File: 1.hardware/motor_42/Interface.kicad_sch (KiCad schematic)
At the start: 0 parts

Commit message: 중간 저장
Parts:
- added C15: 0.1uF/50V, symbol Device:C_Small_US
- added C16: 10uF/16V, symbol Device:C_Small_US
- added U2: MT6816CT, Package_SO:SO-8_3.9x4.9mm_P1.27mm, symbol Sensor_Magnetic:MT6816CT
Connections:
- new net 3V3: C15.1, C16.1, U2.2 (HVPP), U2.4 (VDD)
- new net GND: C15.2, C16.2, U2.8 (GND)
- new net MT6816_CLK: U2.7 (Z/W)
- new net MT6816_CSN: U2.1 (~{CS})
- new net MT6816_MISO: U2.6 (B/V)
- new net MT6816_MOSI: U2.5 (A/U)
- no-connect marks 0 -> 1

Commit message: 중간 저장
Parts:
- added R13: 120/0.1w, symbol Device:R_Small_US
- added U4: TL431AIDBZR, SOT95P237X112-3N, symbol SamacSys_Parts:TL431AIDBZR
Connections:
- net 3V3: now also R13.1
- net GND: now also U4.3 (ANODE)
- net MT6816_CLK renamed SPI1_CLK
- net MT6816_MISO renamed SPI1_MISO
- net MT6816_MOSI renamed SPI1_MOSI
- new net ADC_VREF_2V5: R13.2, U4.1 (CATHODE), U4.2 (REF)
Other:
- moved on the sheet: C15, C16, U2

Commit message: 중간 저장
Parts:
- added C28, C29, C31: 0.1uF/16V, Capacitor_SMD:C_0402_1005Metric, symbol Device:C_Small_US
- added C30: 2.2uF/6.3V, Capacitor_SMD:C_0603_1608Metric, symbol Device:C_Small_US
- added J7: Conn_01x02, symbol Connector_Generic:Conn_01x02
- added LED1: LED_0603_Green_PWR, PCM_LED_SMD_AKL:LED_0603_1608Metric, symbol PCM_LED_AKL:LED_0603_Green
- added LED2: LED_0603_Red_WIFI, PCM_LED_SMD_AKL:LED_0603_1608Metric, symbol PCM_LED_AKL:LED_0603_Red
- added LED3: LED_0603_Blue_BLE, PCM_LED_SMD_AKL:LED_0603_1608Metric, symbol PCM_LED_AKL:LED_0603_Blue
- added R20, R22, R25, R26, R27: 4.7K/0.063w, Resistor_SMD:R_0402_1005Metric, symbol Device:R_Small_US
- added R21, R28: 10K/0.063w, Resistor_SMD:R_0402_1005Metric, symbol Device:R_Small_US
- added R23, R24: NC_0R/0.1w, Resistor_SMD:R_0402_1005Metric, symbol Device:R_Small_US
- added SW3, SW4: SW_Push, mylib:TSB008A2530A, symbol Switch:SW_Push
- added U6: ESP32-C3-WROOM-02, RF_Module:ESP32-C3-WROOM-02, symbol RF_Module:ESP32-C3-WROOM-02
- renumbered C16 to C26, C15 to C27, R13 to R19, U2 to U4, U4 to U5
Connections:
- net 3V3: now also R21.1, R28.1
- net GND: now also C28.2, C29.2, C30.2, C31.2, J7.2 (Pin_2), LED1.1 (K), SW3.2, SW4.2, U6.19 (GND), U6.9 (GND)
- new net: LED3.2 (A), R26.2
- new net: R23.2, U6.13 (IO18)
- new net: LED1.2 (A), R20.2
- new net: LED2.2 (A), R25.2
- new net: LED2.1 (K), U6.4 (IO5)
- new net: LED3.1 (K), U6.3 (IO4)
- new net: R24.2, U6.14 (IO19)
- new net 3V3_MCU: C29.1, C30.1, R20.1, R22.1, R25.1, R26.1, R27.1, U6.1 (3V3)
- new net ACT_BTN: C31.1, R28.2, SW4.1, U6.15 (IO3)
- new net BOOT_BTN: J7.1 (Pin_1), U6.8 (IO9)
- new net D+: R24.1
- new net D-: R23.1
- new net EN_BTN: C28.1, R21.2, SW3.1, U6.2 (EN)
- new net ESP32_UART_RX: R27.2, U6.18 (IO0)
- new net ESP32_UART_TX: R22.2, U6.17 (IO1)
- new net ESP_RX0: U6.11 (IO20/RXD)
- new net ESP_TX0: U6.12 (IO21/TXD)
- new net FSPICLK: U6.5 (IO6)
- new net FSPICSO: U6.10 (IO10)
- new net FSPID: U6.6 (IO7)
- new net FSPIQ: U6.16 (IO2)
- no-connect marks 1 -> 2
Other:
- note added: "BLE/WIFI"
- note added: "EN RESET - up trigger IO9 BOOT - weak pull up"

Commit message: 회로도 대충 완성
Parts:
- removed SW3, SW4: SW_Push, mylib:TSB008A2530A, symbol Switch:SW_Push
- added S3, S4: TSB008A2518A, SamacSys_Parts:TSB008A2518A, symbol SamacSys_Parts:TSB008A2518A
- U4: renamed from U5; footprint SOT95P237X112-3N -> SamacSys_Parts:SOT95P237X112-3N
- renumbered C26 to C28, C31 to C29, C27 to C30, C28 to C31, C29 to C32, C30 to C33, J7 to J8, LED1 to LED3, LED2 to LED4, LED3 to LED5, R20 to R27, R25 to R28, R19 to R29, R28 to R30, R26 to R31, R21 to R32, R27 to R33, R22 to R34, R23 to R35, R24 to R36, U4 to U5
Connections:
- net ACT_BTN: now also S4.1 (COM)
- net EN_BTN: now also S3.1 (COM)
- net GND: now also S3.2 (NO), S4.2 (NO)
- net D+ renamed USB_DP
- net D- renamed USB_DM
- net FSPICLK: no longer names the net of U6.5 (IO6)
- net FSPICSO: no longer names the net of U6.10 (IO10)
- net FSPID: no longer names the net of U6.6 (IO7)
- net FSPIQ: no longer names the net of U6.16 (IO2)
- no-connect marks 2 -> 6
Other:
- moved on the sheet: C29, C31, J8, R30, R32

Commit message: 수정
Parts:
- C28: value 10uF/16V -> 10uF/6.3V; footprint (none) -> Capacitor_SMD:C_0603_1608Metric
- C30: footprint (none) -> Capacitor_SMD:C_0402_1005Metric
- J8: value Conn_01x02 -> BOOT_EN; footprint (none) -> Connector_PinHeader_2.54mm:PinHeader_1x02_P2.54mm_Vertical
- R29: footprint (none) -> Resistor_SMD:R_0603_1608Metric
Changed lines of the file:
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@@
 			)
 		)
-		(property "Value" "Conn_01x02"
+		(property "Value" "BOOT_EN"
 			(at 152.4 165.0999 90)
 			(effects
@@
 			)
 		)
-		(property "Footprint" ""
+		(property "Footprint" "Connector_PinHeader_2.54mm:PinHeader_1x02_P2.54mm_Vertical"
 			(at 147.32 163.83 0)
 			(effects
@@
 			)
 		)
-		(property "Value" "10uF/16V"
+		(property "Value" "10uF/6.3V"
 			(at 33.528 35.052 0)
 			(effects
@@
 			)
 		)
-		(property "Footprint" ""
+		(property "Footprint" "Capacitor_SMD:C_0603_1608Metric"
 			(at 33.02 33.02 0)
 			(effects
@@
 			)
 		)
-		(property "Footprint" ""
+		(property "Footprint" "Capacitor_SMD:C_0402_1005Metric"
 			(at 44.45 33.02 0)
 			(effects
@@
 			)
 		)
-		(property "Footprint" ""
+		(property "Footprint" "Resistor_SMD:R_0603_1608Metric"
 			(at 48.26 68.58 0)
 			(effects

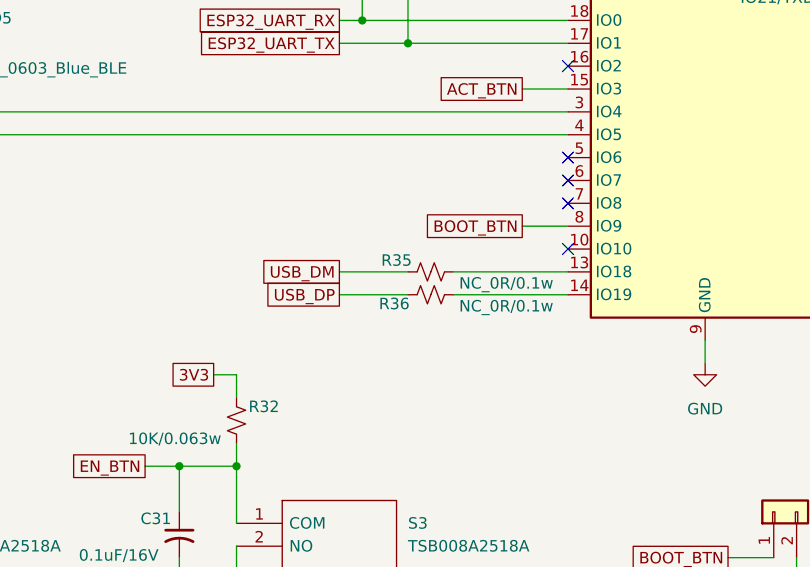
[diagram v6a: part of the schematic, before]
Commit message: 3V3 LDO변경 및 대략적 위치 세팅
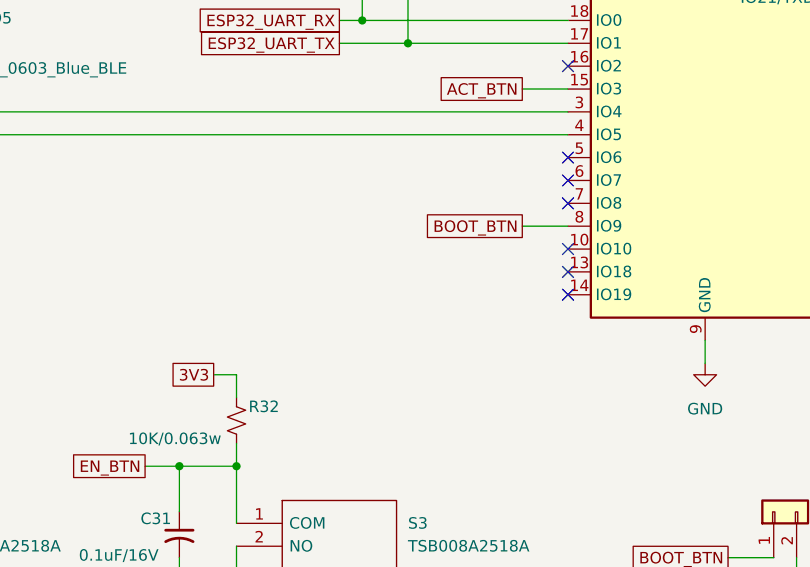
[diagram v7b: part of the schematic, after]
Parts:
- removed R35, R36: NC_0R/0.1w, Resistor_SMD:R_0402_1005Metric, symbol Device:R_Small_US
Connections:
- no-connect marks 6 -> 8
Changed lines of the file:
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@@
 	)
 	(no_connect
+		(at 124.46 139.7)
+	)
+	(no_connect
 		(at 124.46 134.62)
 	)
@@
 		(at 124.46 127)
 	)
+	(no_connect
+		(at 124.46 137.16)
+	)
 	(wire
 		(pts
@@
 	(wire
 		(pts
-			(xy 99.06 139.7) (xy 106.68 139.7)
-		)
-		(stroke
-			(width 0)
-			(type default)
-		)
-	)
-	(wire
-		(pts
 			(xy 142.24 168.91) (xy 147.32 168.91)
 		)
@@
 	(wire
 		(pts
-			(xy 111.76 137.16) (xy 124.46 137.16)
-		)
-		(stroke
-			(width 0)
-			(type default)
-		)
-	)
-	(wire
-		(pts
 			(xy 35.56 148.59) (xy 35.56 151.13)
 		)
@@
 	(wire
 		(pts
-			(xy 111.76 139.7) (xy 124.46 139.7)
-		)
-		(stroke
-			(width 0)
-			(type default)
-		)
-	)
-	(wire
-		(pts
 			(xy 35.56 156.21) (xy 35.56 158.75)
 		)
@@
 	(wire
 		(pts
-			(xy 99.06 137.16) (xy 106.68 137.16)
-		)
-		(stroke
-			(width 0)
-			(type default)
-		)
-	)
-	(wire
-		(pts
 			(xy 77.47 158.75) (xy 81.28 158.75)
 		)
@@
 		)
 	)
-	(global_label "USB_DM"
-		(shape passive)
-		(at 99.06 137.16 180)
-		(fields_autoplaced yes)
-		(effects
-			(font
-				(size 1.27 1.27)
-			)
-			(justify right)
-		)
-		(property "Intersheetrefs" "${INTERSHEET_REFS}"
-			(at 89.6871 137.16 0)
-			(effects
-				(font
-					(size 1.27 1.27)
-				)
-				(justify right)
-				(hide yes)
-			)
-		)
-	)
-	(global_label "USB_DP"
-		(shape passive)
-		(at 99.06 139.7 180)
-		(fields_autoplaced yes)
-		(effects
-			(font
-				(size 1.27 1.27)
-			)
-			(justify right)
-		)
-		(property "Intersheetrefs" "${INTERSHEET_REFS}"
-			(at 89.8685 139.7 0)
-			(effects
-				(font
-					(size 1.27 1.27)
-				)
-				(justify right)
-				(hide yes)
-			)
-		)
-	)
 	(global_label "EN_BTN"
 		(shape passive)
@@
 	)
 	(symbol
-		(lib_id "Device:R_Small_US")
-		(at 109.22 137.16 90)
-		(unit 1)
-		(exclude_from_sim no)
-		(in_bom yes)
-		(on_board yes)
-		(dnp no)
-		(property "Reference" "R35"
-			(at 105.41 135.89 90)
-			(effects
-				(font
-					(size 1.27 1.27)
-				)
-			)
-		)
-		(property "Value" "NC_0R/0.1w"
-			(at 117.602 138.43 90)
-			(effects
-				(font
-					(size 1.27 1.27)
-				)
-			)
-		)
-		(property "Footprint" "Resistor_SMD:R_0402_1005Metric"
-			(at 109.22 137.16 0)
-			(effects
-				(font
-					(size 1.27 1.27)
-				)
-				(hide yes)
-			)
-		)
-		(property "Datasheet" "~"
-			(at 109.22 137.16 0)
-			(effects
-				(font
-					(size 1.27 1.27)
-				)
-				(hide yes)
-			)
-		)
-		(property "Description" "Resistor, small US symbol"
-			(at 109.22 137.16 0)
-			(effects
-				(font
-					(size 1.27 1.27)
-				)
-				(hide yes)
-			)
-		)
-		(pin "2"
-		)
-		(pin "1"
-		)
-		(instances
-			(project "motor_42"
-				(path "/3c5de6a8-6840-43a5-a2fb-24dbb7f0450d/9b49f0d1-725c-46a9-83d3-f1e791b8bf0d"
-					(reference "R35")
-					(unit 1)
-				)
-			)
-		)
-	)
-	(symbol
 		(lib_id "PCM_LED_AKL:LED_0603_Green")
 		(at 30.48 106.68 270)
@@
 					(unit 1)
 				)
-			)
-		)
-	)
-	(symbol
-		(lib_id "Device:R_Small_US")
-		(at 109.22 139.7 90)
-		(unit 1)
-		(exclude_from_sim no)
-		(in_bom yes)
-		(on_board yes)
-		(dnp no)
-		(property "Reference" "R36"
-			(at 105.156 140.716 90)
-			(effects
-				(font
-					(size 1.27 1.27)
-				)
-			)
-		)
-		(property "Value" "NC_0R/0.1w"
-			(at 117.602 140.97 90)
-			(effects
-				(font
-					(size 1.27 1.27)
-				)
-			)
-		)
-		(property "Footprint" "Resistor_SMD:R_0402_1005Metric"
-			(at 109.22 139.7 0)
-			(effects
-				(font
-					(size 1.27 1.27)
-				)
-				(hide yes)
-			)
-		)
-		(property "Datasheet" "~"
-			(at 109.22 139.7 0)
-			(effects
-				(font
-					(size 1.27 1.27)
-				)
-				(hide yes)
-			)
-		)
-		(property "Description" "Resistor, small US symbol"
-			(at 109.22 139.7 0)
-			(effects
-				(font
-					(size 1.27 1.27)
-				)
-				(hide yes)
-			)
-		)
-		(pin "2"
-		)
-		(pin "1"
-		)
-		(instances
-			(project "motor_42"
-				(path "/3c5de6a8-6840-43a5-a2fb-24dbb7f0450d/9b49f0d1-725c-46a9-83d3-f1e791b8bf0d"
-					(reference "R36")
-					(unit 1)
-				)

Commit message: 중간 저장
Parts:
- removed C29: 0.1uF/16V, Capacitor_SMD:C_0402_1005Metric, symbol Device:C_Small_US
- removed R30: 10K/0.063w, Resistor_SMD:R_0402_1005Metric, symbol Device:R_Small_US
- removed S4: TSB008A2518A, SamacSys_Parts:TSB008A2518A, symbol SamacSys_Parts:TSB008A2518A
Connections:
- net ACT_BTN: no longer names the net of U6.15 (IO3)
- no-connect marks 8 -> 9
